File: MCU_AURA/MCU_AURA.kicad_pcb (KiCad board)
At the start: 4 copper layers, 112 parts, among them J100 XT30PW-M, J101 USB_C_Receptacle_USB2.0_16P, J200 TC2050-IDC-430, J300 TF-CARD_H1.8, J500 Screw_Terminal_01x04, J502 532617006, J504 532617004, J505 532617004, Q300 BSS138, Q301 BSS138, Q302 BSS138, U100 TPS56C230RJER, U101 SI4825DDY-T1-GE3, U102 TPS2115ADRBR, U103 TLV62566DBVR, U104 AP2127N-1.8, U200 ESP32-S3-WROOM-1, U201 USBLC6-2SC6, U300 ICM-20948, U301 BMP280, U500 DMN6040SSD-13

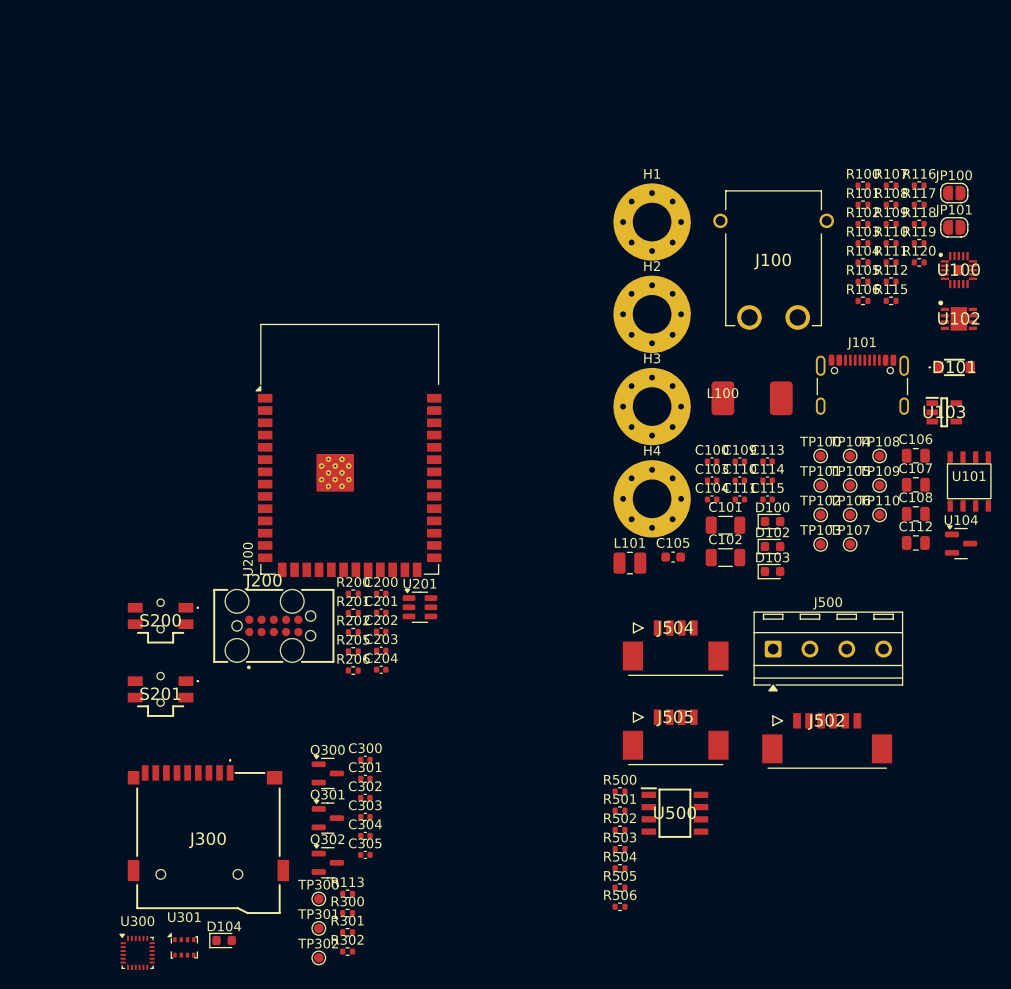
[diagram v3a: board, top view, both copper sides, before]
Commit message: Adding 3D Models
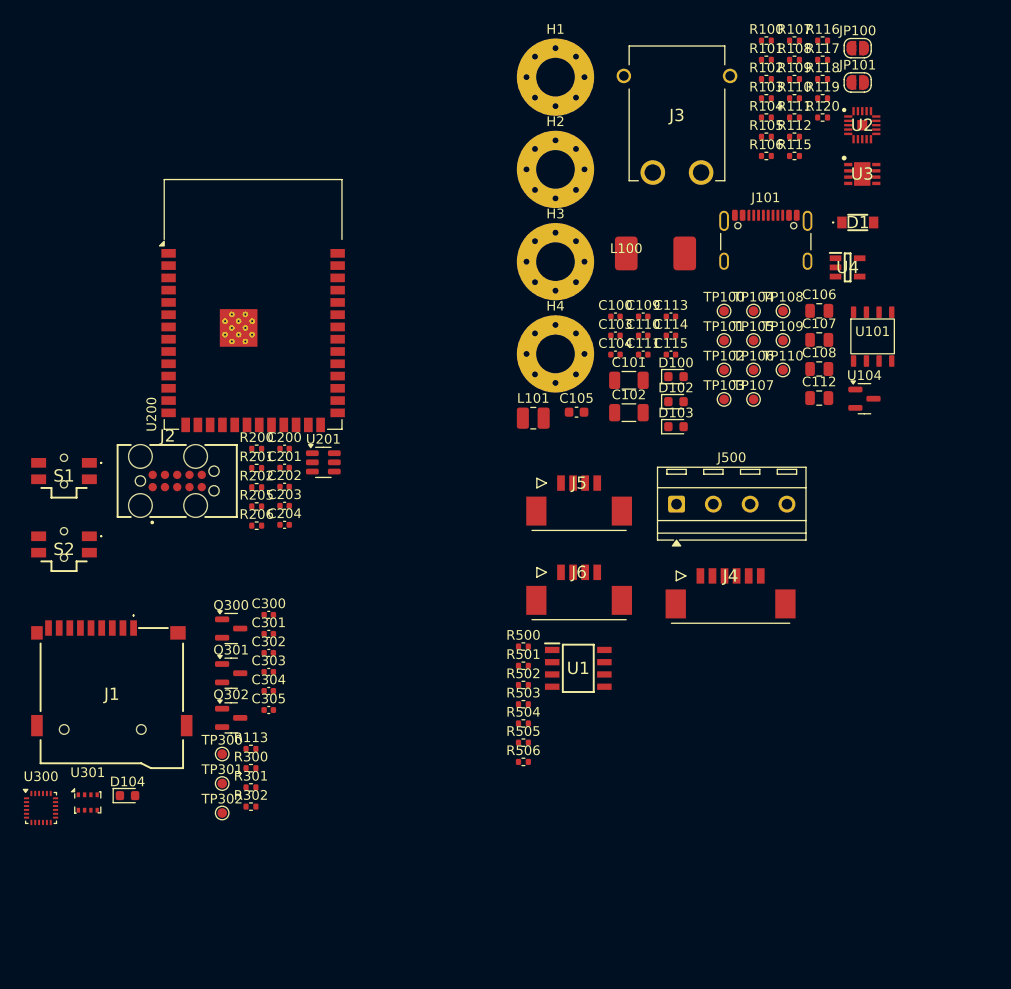
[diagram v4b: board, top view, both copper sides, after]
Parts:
- removed D101: MMSZ5242B, MMSZ5252B:MMSZ5252B
- removed J100: XT30PW-M, XT30PWM:XT30PWM
- removed J200: TC2050-IDC-430, TC2050-IDC:TC2050-IDC
- removed J300: TF-CARD_H1.8, TF-CARD_H1_8:TFCARDH18
- removed J502: 532617006, 532617006:532617006
- removed J504, J505: 532617004, 532617004:532617004
- removed S200, S201: EVQ-PUC02K, EVQ-PUC02k:EVQPUC02K
- removed U100: TPS56C230RJER, TPS56C230RJER:QFN45P300X300X100-21N-D
- removed U102: TPS2115ADRBR, TPS2115ADRBR:SON65P300X300X100-9N-D
- removed U103: TLV62566DBVR, TLV62566DBVR:SOT95P280X145-5N
- removed U500: DMN6040SSD-13, DMN6040SSD-13:SOIC127P600X170-8N
- added D1: MMSZ5242B, MMSZ5252B:MMSZ5252B, F.Cu at (146.5, 65.7)
- added J1: TF-CARD_H1.8, TF-CARD_H1_8:TFCARDH18, F.Cu at (69.3, 114.9)
- added J2: TC2050-IDC-430, TC2050-IDC:TC2050-IDC, F.Cu at (75.1, 89.9)
- added J3: XT30PW-M, XT30PWM:XT30PWM, F.Cu at (127.8, 54.6)
- added J4: 532617006, 532617006:532617006, F.Cu at (133.3, 102.2)
- added J5: 532617004, 532617004:532617004, F.Cu at (117.6, 92.6)
- added J6: 532617004, 532617004:532617004, F.Cu at (117.6, 101.9)
- added S1: EVQ-PUC02K, EVQ-PUC02k:EVQPUC02K, F.Cu at (64.3, 91.4)
- added S2: EVQ-PUC02K, EVQ-PUC02k:EVQPUC02K, F.Cu at (64.3, 99.0)
- added U1: DMN6040SSD-13, DMN6040SSD-13:SOIC127P600X170-8N, F.Cu at (117.6, 111.8)
- added U2: TPS56C230RJER, TPS56C230RJER:QFN45P300X300X100-21N-D, F.Cu at (147.0, 55.6)
- added U3: TPS2115ADRBR, TPS2115ADRBR:SON65P300X300X100-9N-D, F.Cu at (147.0, 60.6)
- added U4: TLV62566DBVR, TLV62566DBVR:SOT95P280X145-5N, F.Cu at (145.4, 70.3)
- moved D104 18.0 mm to (70.9, 125.0)
- moved R504 18.0 mm to (111.9, 117.5)
- moved TP301 18.0 mm to (80.7, 123.7)
- moved U301 18.0 mm to (66.8, 125.7)
- moved D100 18.0 mm to (127.7, 81.6)
- moved D102 18.0 mm to (127.7, 84.2)
- moved D103 18.0 mm to (127.7, 86.8)
- moved H1 18.0 mm to (115.2, 50.6)
- moved J500 18.0 mm to (127.7, 94.8)
- moved R105 18.0 mm to (137.0, 56.8)
- moved R112 18.0 mm to (139.9, 56.8)
- moved U300 18.0 mm to (61.9, 126.3)
- moved C101 18.0 mm to (122.8, 82.0)
- moved C102 18.0 mm to (122.8, 85.3)
- moved C105 18.0 mm to (117.4, 85.3)
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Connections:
- net RX renamed GPS_RX
- net TX renamed GPS_TX
- R113 pad 1: AUX_CS_LED -> LED
